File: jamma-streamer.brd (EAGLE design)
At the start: 180.3 x 92 mm, 65 parts, among them IC1 LM7805, J1 Audio line out, J2 ICSP, J3 796136-1, J4 DM3AT-SF-PEJM5, J5 KMMX-BSMT35S-B30TR, T1 TY-145P, T2 TY-145P, U1 CD74HC165MD16-M, U10 LM358DTD8-M, U2 ATMEGA328PB-AUR, U3 74HC4050D, U4 TLV757X / LP298X, U5 CD74HC165MD16-M, U6 CD74HC165MD16-M, U7 FT232RL, U8 DS3231SNT&R21-0042B_16-M, U9 NDT2955SOT-223-M, Y1 16MHz

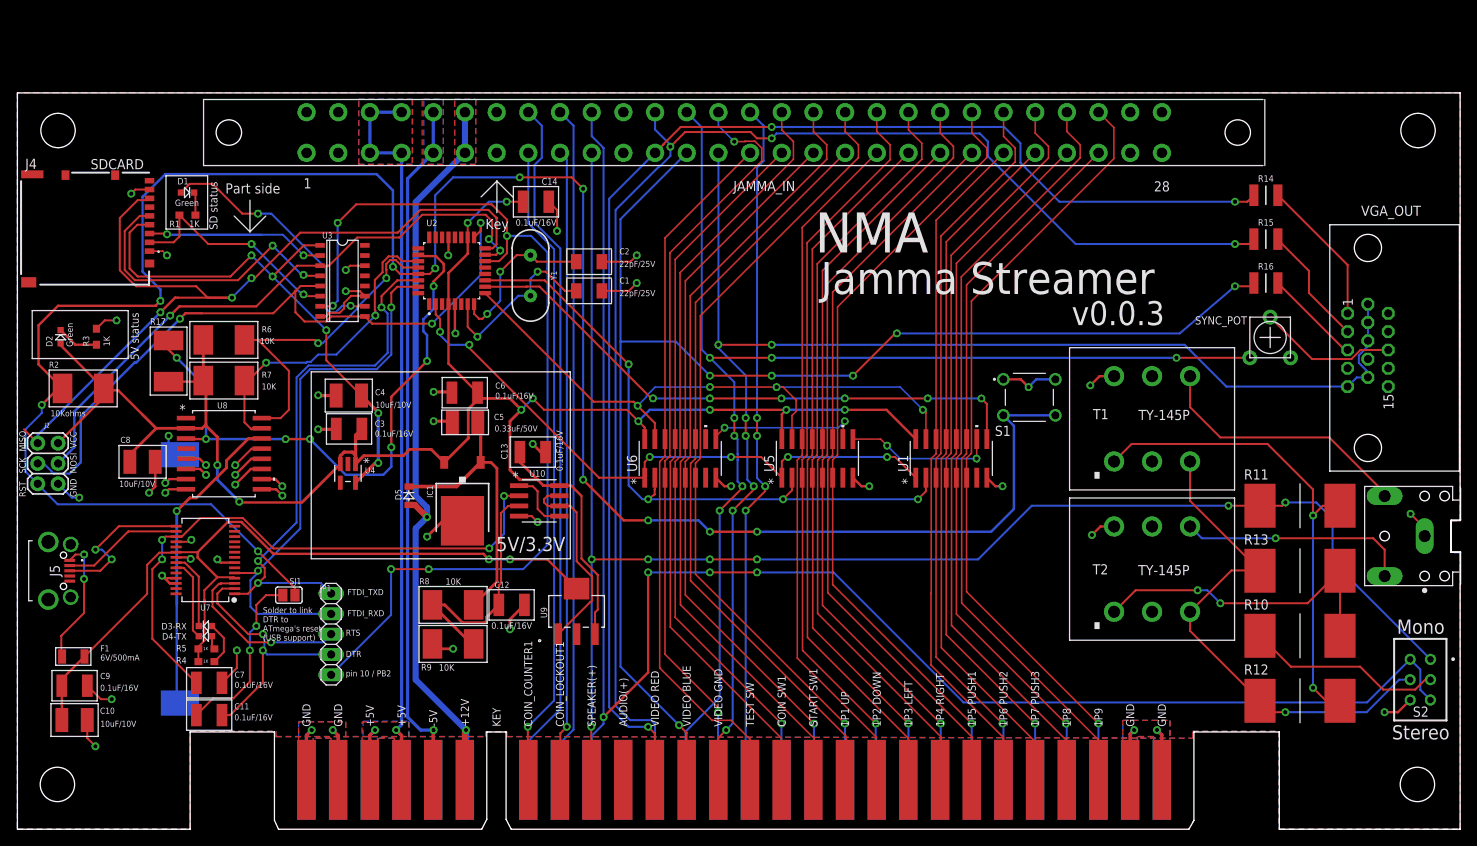
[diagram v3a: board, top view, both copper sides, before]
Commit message: Finalization + add jamma connector horiz
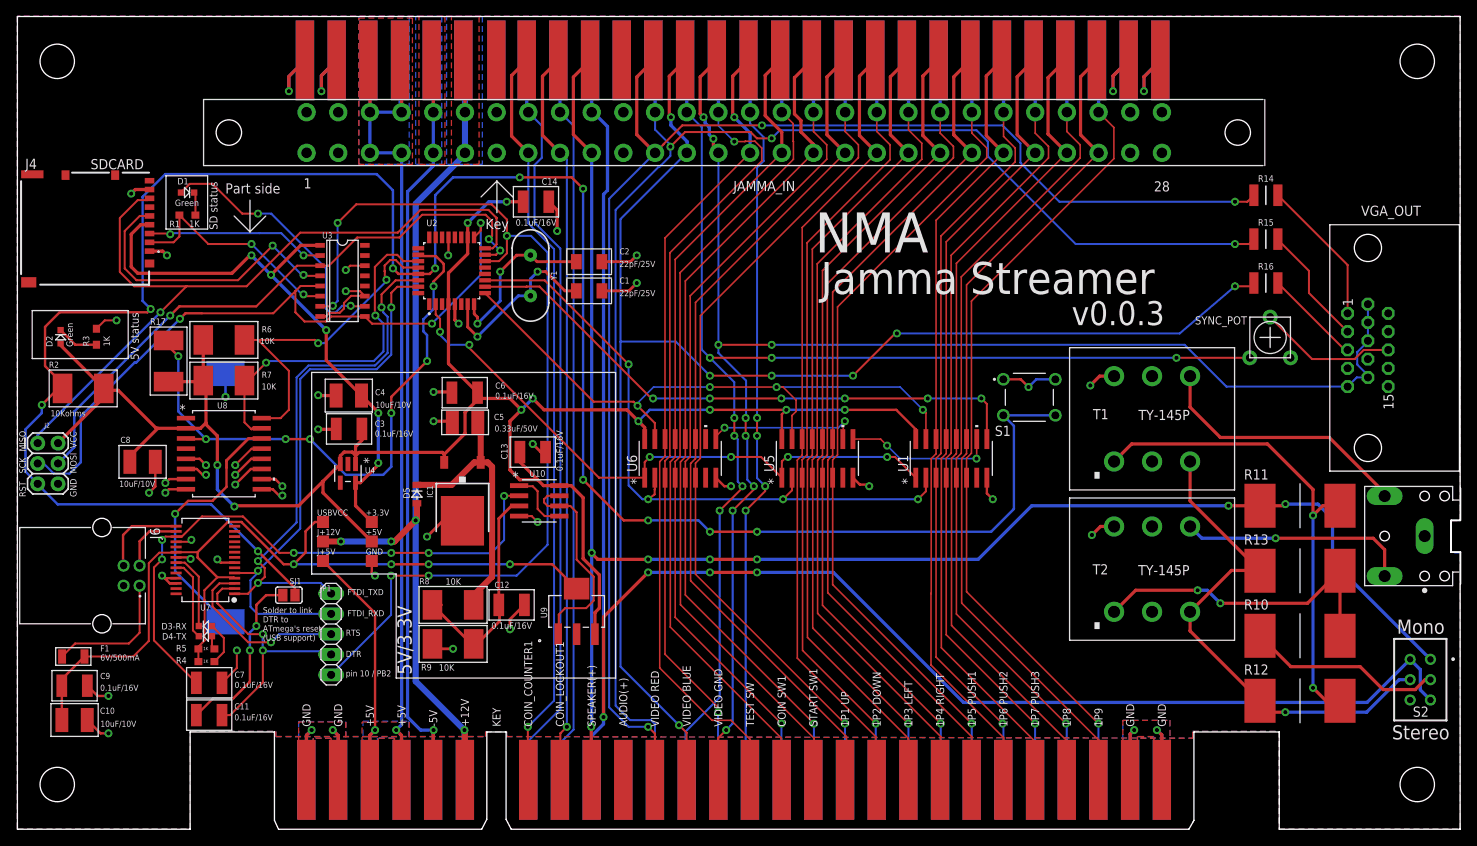
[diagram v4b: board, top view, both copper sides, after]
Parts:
- removed J5: KMMX-BSMT35S-B30TR, nma-eagle:KMMXBSMT35SB30TR
- added +3.3V, +5V, GND, J+12V, J+5V, USBVCC: PTR1TP15SQ, testpad:TP15SQ
- added J6: 292304-1, nma-eagle:TE_292304-1
- added JA1: JAMMA_HORIZ_TOP, nma-eagle:JAMMA_HORIZ_TOP
- added U$1: JAMMA_HORIZ_BOTTOM, nma-eagle:JAMMA_HORIZ_BOTTOM
- moved J3 11.6 mm to (26.0, 41.5)
- moved D5 1.04 mm to (49.9, 41.9)
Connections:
- new net 11: JA1.11
- net 15: now also JA1.15
- net 16: now also JA1.16
- net 17: now also JA1.17
- net 18: now also JA1.18
- net 19: now also JA1.19
- net 20: now also JA1.20
- net 21: now also JA1.21
- net 22: now also JA1.22
- net 23: now also JA1.23
- net 24: now also JA1.24
- net 25: now also JA1.25
- net 26: now also JA1.26
- net 8: now also JA1.8
- net 9: now also JA1.9
- net BLUE: now also JA1.13
- net D+: now also J6.3; no longer J5.3
- net D-: now also J6.2; no longer J5.2
- net GND: now also GND.TP, J6.4, JA1.1, JA1.2, JA1.27, JA1.28, U$1.A, U$1.B, U$1._E, U$1._F; no longer J5.5, J5.MH1, J5.MH2, J5.MH3, J5.MH4
- net GREEN: now also U$1.N
- net J: now also U$1.J
- net JAMMA+12V: now also J+12V.TP, JA1.6, U$1.F
- net JAMMA+5V: now also J+5V.TP, JA1.3, JA1.4, U$1.C, U$1.D
- net JAMMA-5V: now also JA1.5, U$1.E
- net K: now also U$1.K
- net P: now also U$1.P
- net R: now also U$1.R
- net RED: now also JA1.12
- net S: now also U$1.S
- net SPK+: now also JA1.10
- net SPK-: now also U$1.L
- net T: now also U$1.T
- net U: now also U$1.U
- net USBVCC: now also USBVCC.TP
- net USB_V: now also J6.1; no longer J5.1
- net V: now also U$1.V
- net VCC: now also +5V.TP
- net VCC_2: now also +3.3V.TP
- net VGROUND: now also JA1.14
- net W: now also U$1.W
- net X: now also U$1.X
- net Y: now also U$1.Y
- net Z: now also U$1.Z
- net _A: now also U$1._A
- net _B: now also U$1._B
- net _C: now also U$1._C
- net _D: now also U$1._D
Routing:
- net JAMMA+5V: track 111.4 -> 161.5 mm
- net GND: track 208.5 -> 235.8 mm, vias 50 -> 52
- net JAMMA+12V: track 99.4 -> 123.2 mm, vias 2 -> 4
- net SPK+: track 197.5 -> 211.0 mm
- net RED: track 166.4 -> 180.0 mm
- net VGROUND: track 176.0 -> 189.6 mm, vias 7 -> 9
- net 17: track 92.2 -> 105.7 mm
- net 25: track 90.3 -> 103.8 mm
- net 18: track 94.5 -> 107.9 mm
- net 20: track 88.8 -> 102.2 mm
- net 22: track 93.3 -> 106.7 mm
- net 24: track 88.1 -> 101.5 mm
- net 26: track 92.6 -> 105.9 mm
- net BLUE: track 170.7 -> 184.0 mm, vias 6 -> 7
- net 9: track 79.1 -> 92.4 mm
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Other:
- board size 180.3 x 92 mm -> 180.3 x 101.6 mm

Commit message: DRC Sparkfun ok
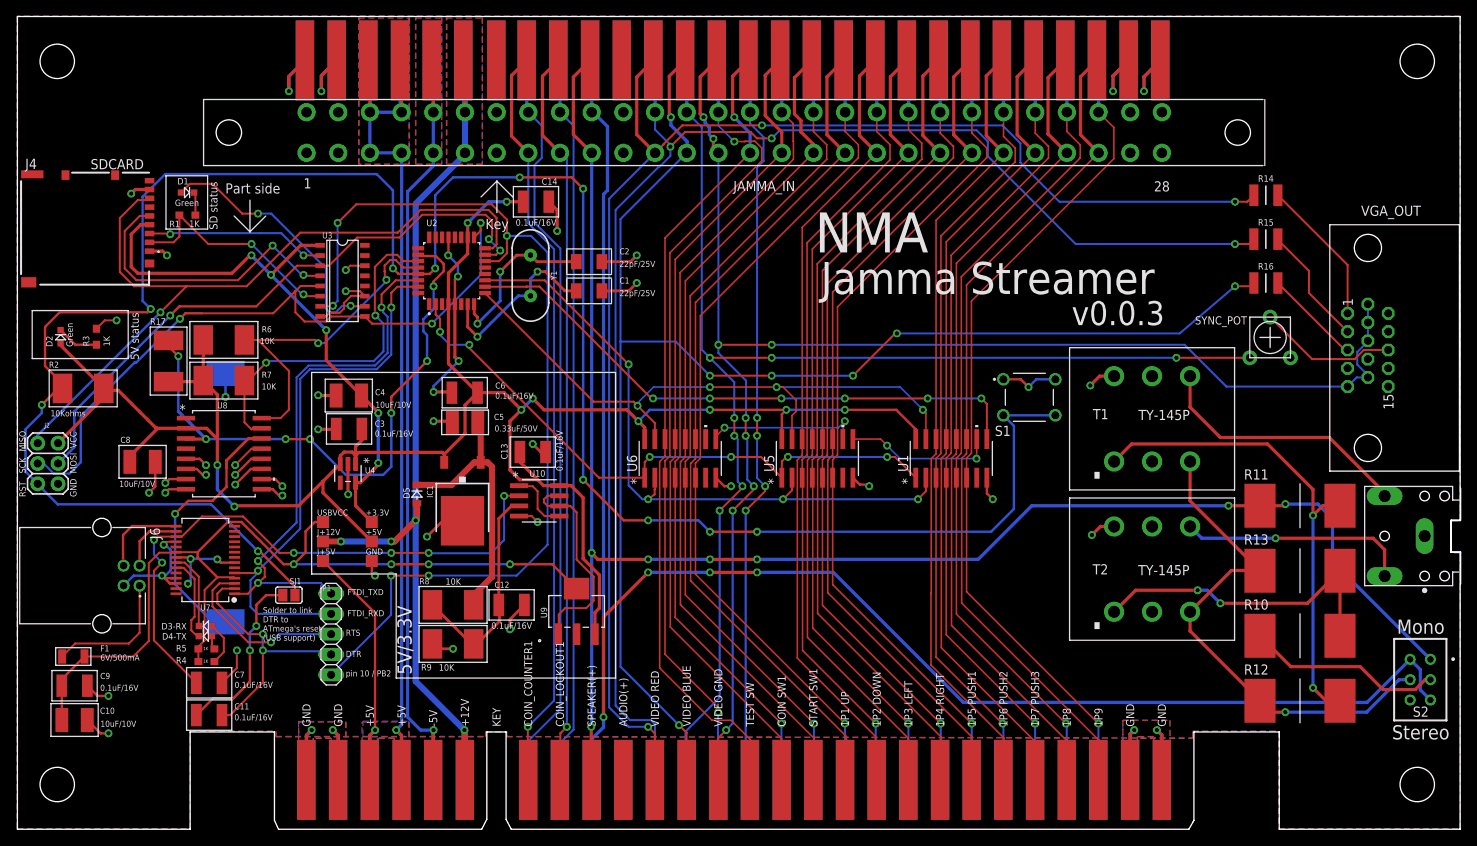
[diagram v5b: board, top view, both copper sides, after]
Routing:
- net GND: track 235.8 -> 272.7 mm, vias 52 -> 55
- net VCC: track 260.8 -> 264.1 mm
- net VCC33: track 74.4 -> 75.9 mm
- net CMP: track 28.8 -> 27.6 mm
- net N$31: track 32.8 -> 33.7 mm
